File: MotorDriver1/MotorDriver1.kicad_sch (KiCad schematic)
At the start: 14 parts, among them J1 REPLACE W STM I/O PIN CONN, J2 REPLACE W STM I/O PIN CONN, Q1 IRLZ44N, Q2 IRLZ44N

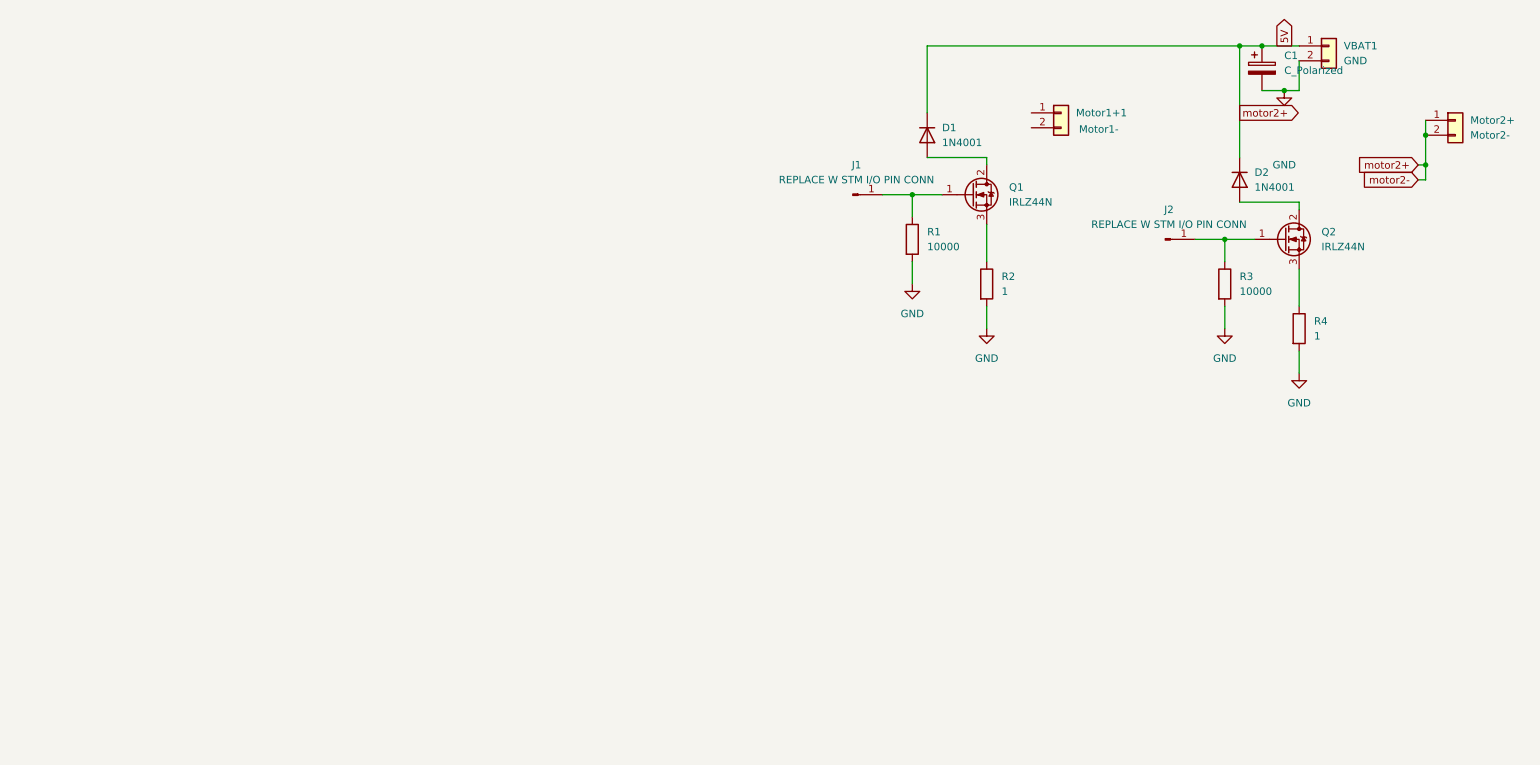
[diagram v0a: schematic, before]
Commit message: Set up KiCad libraries & STM32 page
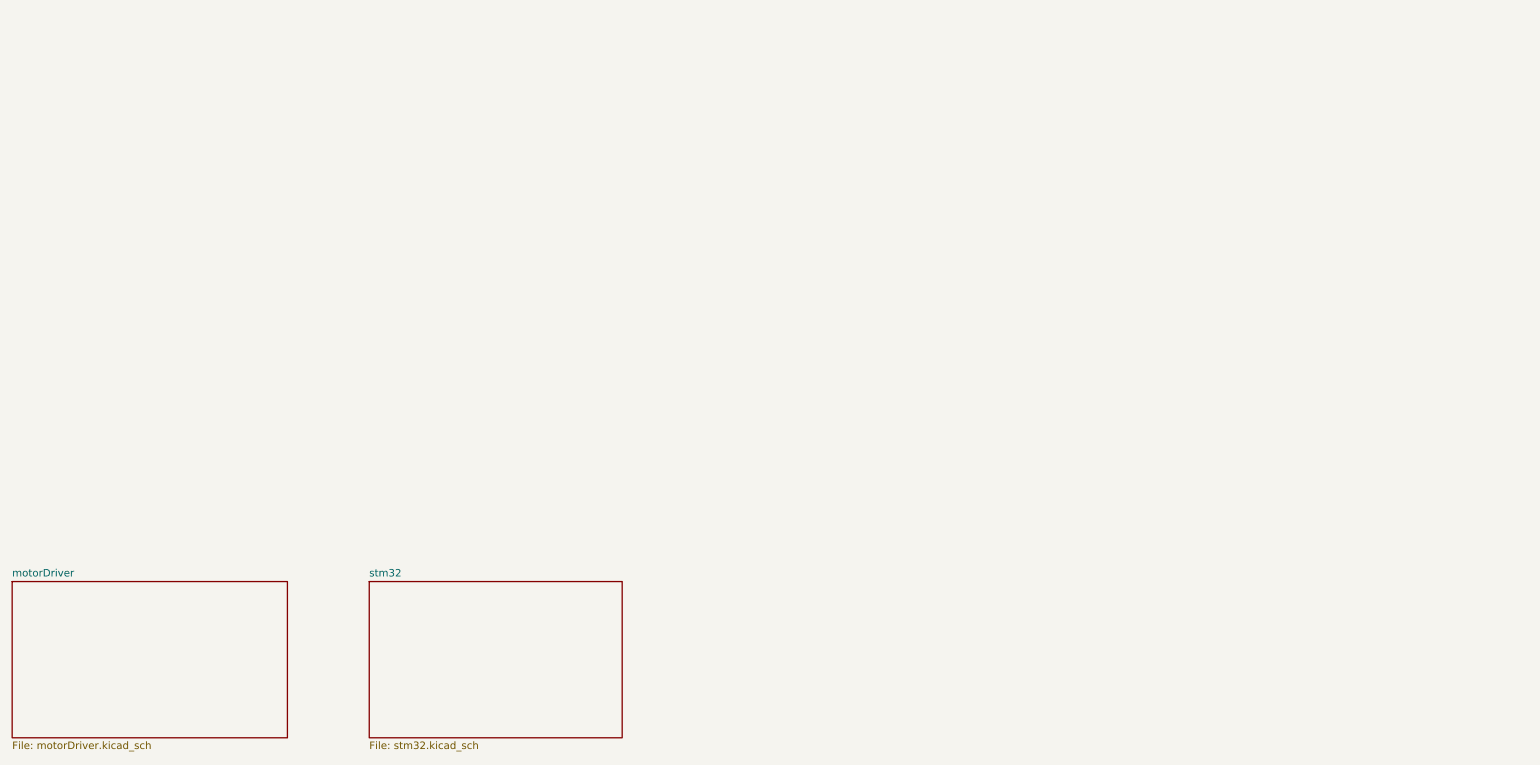
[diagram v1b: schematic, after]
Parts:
- removed C1: C_Polarized, symbol Device:C_Polarized
- removed D1, D2: 1N4001, Diode_THT:D_DO-41_SOD81_P10.16mm_Horizontal, symbol Diode:1N4001
- removed J1, J2: REPLACE W STM I/O PIN CONN, symbol Connector:Conn_01x01_Pin
- removed Motor1+1: Motor1-, symbol Connector_Generic:Conn_01x02
- removed Motor2+: Motor2-, symbol Connector_Generic:Conn_01x02
- removed Q1, Q2: IRLZ44N, Package_TO_SOT_THT:TO-220-3_Vertical, symbol Transistor_FET:IRLZ44N
- removed R1, R3: 10000, symbol Device:R
- removed R2, R4: 1, symbol Device:R
- removed VBAT1: GND, symbol Connector_Generic:Conn_01x02
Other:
- added sheet motorDriver (motorDriver.kicad_sch)
- added sheet stm32 (stm32.kicad_sch)

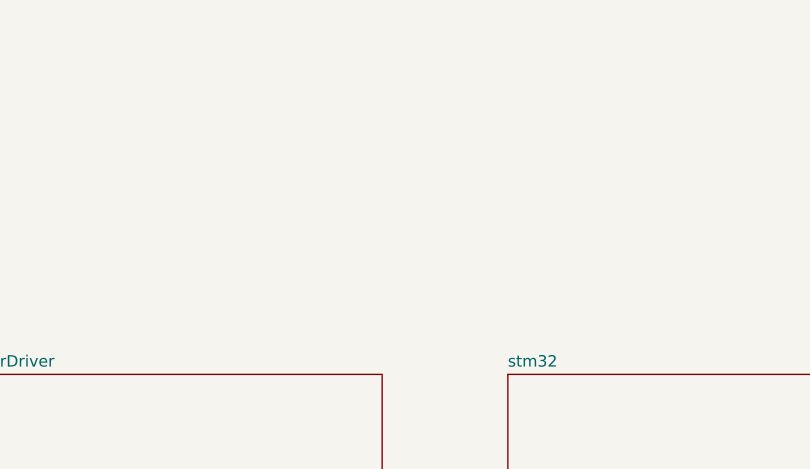
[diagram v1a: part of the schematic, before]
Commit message: added pressure sensor and flags to STM need op amp rails
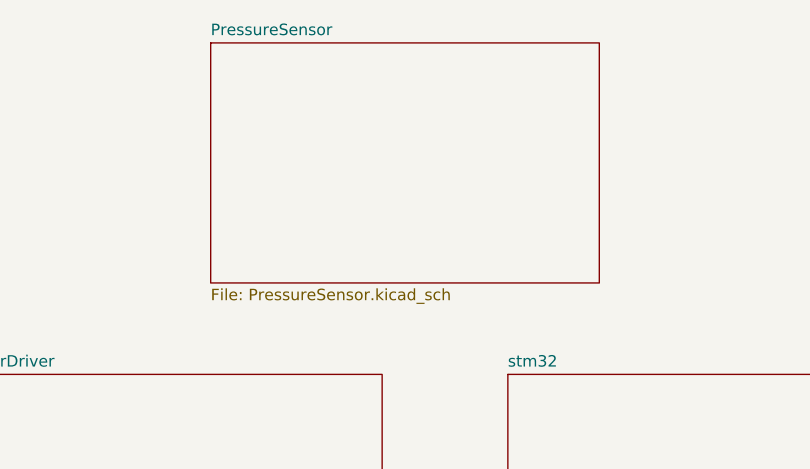
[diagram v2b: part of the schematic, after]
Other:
- added sheet PressureSensor (PressureSensor.kicad_sch)
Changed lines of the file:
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@@
 	(paper "A4")
+	(sheet
+		(at 52.07 118.11)
+		(size 43.18 26.67)
+		(exclude_from_sim no)
+		(in_bom yes)
+		(on_board yes)
+		(dnp no)
+		(fields_autoplaced yes)
+		(stroke
+			(width 0.1524)
+			(type solid)
+		)
+		(fill
+			(color 0 0 0 0.0000)
+		)
+		(property "Sheetname" "PressureSensor"
+			(at 52.07 117.3984 0)
+			(effects
+				(font
+					(size 1.27 1.27)
+				)
+				(justify left bottom)
+			)
+		)
+		(property "Sheetfile" "PressureSensor.kicad_sch"
+			(at 52.07 145.3646 0)
+			(effects
+				(font
+					(size 1.27 1.27)
+				)
+				(justify left top)
+			)
+		)
+		(instances
+			(project "MotorDriver1"
+				(path "/79cc9cfe-04d6-4d00-aa84-feae66cf8c45"
+					(page "4")
+				)
+			)
+		)
+	)
 	(sheet
 		(at 24.13 154.94)

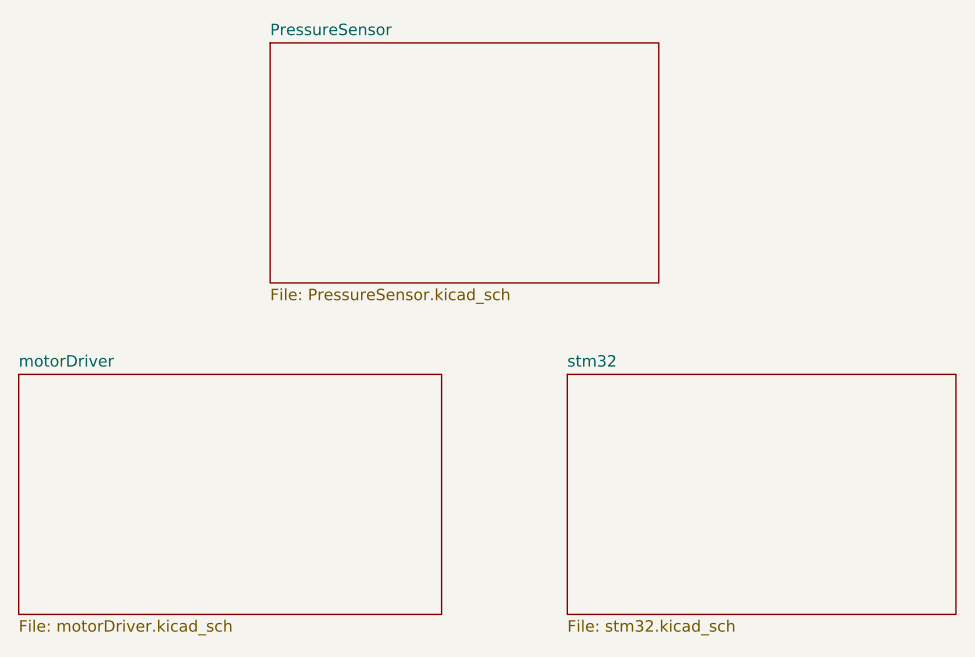
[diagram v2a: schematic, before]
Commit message: missing crystal verification
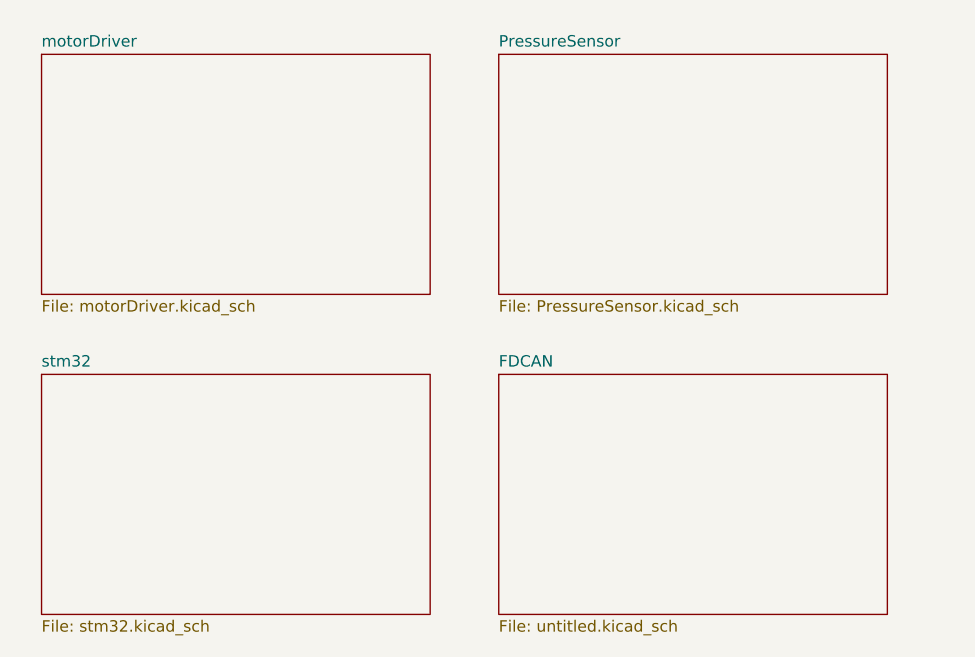
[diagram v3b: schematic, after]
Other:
- added sheet FDCAN (untitled.kicad_sch)
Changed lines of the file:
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@@
 	(paper "A4")
 	(sheet
-		(at 52.07 118.11)
+		(at 77.47 119.38)
 		(size 43.18 26.67)
 		(exclude_from_sim no)
@@
 		)
 		(property "Sheetname" "PressureSensor"
-			(at 52.07 117.3984 0)
+			(at 77.47 118.6684 0)
 			(effects
 				(font
@@
 		)
 		(property "Sheetfile" "PressureSensor.kicad_sch"
-			(at 52.07 145.3646 0)
+			(at 77.47 146.6346 0)
 			(effects
 				(font
@@
 	)
 	(sheet
-		(at 24.13 154.94)
-		(size 46.99 26.67)
+		(at 77.47 154.94)
+		(size 43.18 26.67)
+		(exclude_from_sim no)
+		(in_bom yes)
+		(on_board yes)
+		(dnp no)
+		(fields_autoplaced yes)
+		(stroke
+			(width 0.1524)
+			(type solid)
+		)
+		(fill
+			(color 0 0 0 0.0000)
+		)
+		(property "Sheetname" "FDCAN"
+			(at 77.47 154.2284 0)
+			(effects
+				(font
+					(size 1.27 1.27)
+				)
+				(justify left bottom)
+			)
+		)
+		(property "Sheetfile" "untitled.kicad_sch"
+			(at 77.47 182.1946 0)
+			(effects
+				(font
+					(size 1.27 1.27)
+				)
+				(justify left top)
+			)
+		)
+		(instances
+			(project "MotorDriver1"
+				(path "/79cc9cfe-04d6-4d00-aa84-feae66cf8c45"
+					(page "5")
+				)
+			)
+		)
+	)
+	(sheet
+		(at 26.67 119.38)
+		(size 43.18 26.67)
 		(exclude_from_sim no)
 		(in_bom yes)
@@
 		)
 		(property "Sheetname" "motorDriver"
-			(at 24.13 154.2284 0)
+			(at 26.67 118.6684 0)
 			(effects
 				(font
@@
 		)
 		(property "Sheetfile" "motorDriver.kicad_sch"
-			(at 24.13 182.1946 0)
+			(at 26.67 146.6346 0)
 			(effects
 				(font
@@
 	)
 	(sheet
-		(at 85.09 154.94)
+		(at 26.67 154.94)
 		(size 43.18 26.67)
 		(exclude_from_sim no)
@@
 		)
 		(property "Sheetname" "stm32"
-			(at 85.09 154.2284 0)
+			(at 26.67 154.2284 0)
 			(effects
 				(font
@@
 		)
 		(property "Sheetfile" "stm32.kicad_sch"
-			(at 85.09 182.1946 0)
+			(at 26.67 182.1946 0)
 			(effects
 				(font

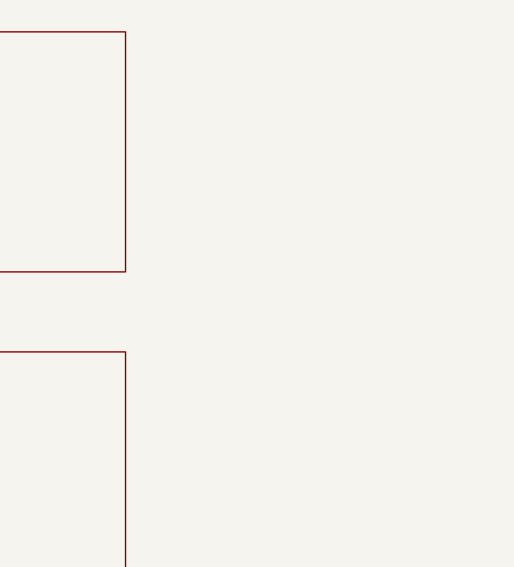
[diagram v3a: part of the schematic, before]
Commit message: Added tooling holes
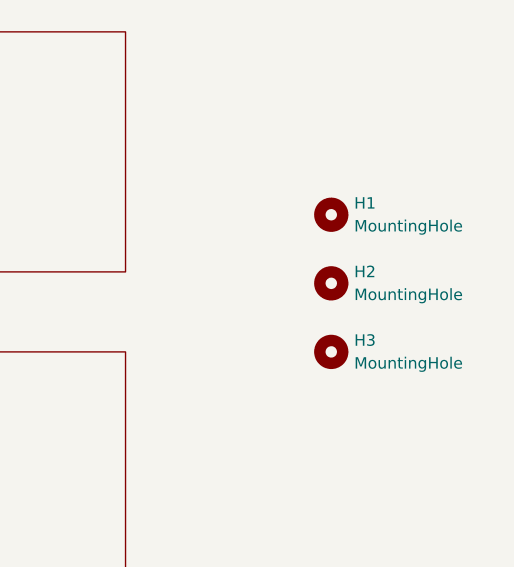
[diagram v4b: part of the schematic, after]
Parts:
- added H1, H2, H3: MountingHole, MountingHole:ToolingHole_1.152mm, symbol Mechanical:MountingHole
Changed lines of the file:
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@@
 	(generator_version "9.0")
 	(paper "A4")
+	(symbol
+		(lib_id "Mechanical:MountingHole")
+		(at 143.51 147.32 0)
+		(unit 1)
+		(exclude_from_sim no)
+		(in_bom no)
+		(on_board yes)
+		(dnp no)
+		(fields_autoplaced yes)
+		(property "Reference" "H2"
+			(at 146.05 146.0499 0)
+			(effects
+				(font
+					(size 1.27 1.27)
+				)
+				(justify left)
+			)
+		)
+		(property "Value" "MountingHole"
+			(at 146.05 148.5899 0)
+			(effects
+				(font
+					(size 1.27 1.27)
+				)
+				(justify left)
+			)
+		)
+		(property "Footprint" "MountingHole:ToolingHole_1.152mm"
+			(at 143.51 147.32 0)
+			(effects
+				(font
+					(size 1.27 1.27)
+				)
+				(hide yes)
+			)
+		)
+		(property "Datasheet" "~"
+			(at 143.51 147.32 0)
+			(effects
+				(font
+					(size 1.27 1.27)
+				)
+				(hide yes)
+			)
+		)
+		(property "Description" "Mounting Hole without connection"
+			(at 143.51 147.32 0)
+			(effects
+				(font
+					(size 1.27 1.27)
+				)
+				(hide yes)
+			)
+		)
+		(instances
+			(project "MotorDriver1"
+				(path "/79cc9cfe-04d6-4d00-aa84-feae66cf8c45"
+					(reference "H2")
+					(unit 1)
+				)
+			)
+		)
+	)
+	(symbol
+		(lib_id "Mechanical:MountingHole")
+		(at 143.51 154.94 0)
+		(unit 1)
+		(exclude_from_sim no)
+		(in_bom no)
+		(on_board yes)
+		(dnp no)
+		(fields_autoplaced yes)
+		(property "Reference" "H3"
+			(at 146.05 153.6699 0)
+			(effects
+				(font
+					(size 1.27 1.27)
+				)
+				(justify left)
+			)
+		)
+		(property "Value" "MountingHole"
+			(at 146.05 156.2099 0)
+			(effects
+				(font
+					(size 1.27 1.27)
+				)
+				(justify left)
+			)
+		)
+		(property "Footprint" "MountingHole:ToolingHole_1.152mm"
+			(at 143.51 154.94 0)
+			(effects
+				(font
+					(size 1.27 1.27)
+				)
+				(hide yes)
+			)
+		)
+		(property "Datasheet" "~"
+			(at 143.51 154.94 0)
+			(effects
+				(font
+					(size 1.27 1.27)
+				)
+				(hide yes)
+			)
+		)
+		(property "Description" "Mounting Hole without connection"
+			(at 143.51 154.94 0)
+			(effects
+				(font
+					(size 1.27 1.27)
+				)
+				(hide yes)
+			)
+		)
+		(instances
+			(project "MotorDriver1"
+				(path "/79cc9cfe-04d6-4d00-aa84-feae66cf8c45"
+					(reference "H3")
+					(unit 1)
+				)
+			)
+		)
+	)
+	(symbol
+		(lib_id "Mechanical:MountingHole")
+		(at 143.51 139.7 0)
+		(unit 1)
+		(exclude_from_sim no)
+		(in_bom no)
+		(on_board yes)
+		(dnp no)
+		(fields_autoplaced yes)
+		(property "Reference" "H1"
+			(at 146.05 138.4299 0)
+			(effects
+				(font
+					(size 1.27 1.27)
+				)
+				(justify left)
+			)
+		)
+		(property "Value" "MountingHole"
+			(at 146.05 140.9699 0)
+			(effects
+				(font
+					(size 1.27 1.27)
+				)
+				(justify left)
+			)
+		)
+		(property "Footprint" "MountingHole:ToolingHole_1.152mm"
+			(at 143.51 139.7 0)
+			(effects
+				(font
+					(size 1.27 1.27)
+				)
+				(hide yes)
+			)
+		)
+		(property "Datasheet" "~"
+			(at 143.51 139.7 0)
+			(effects
+				(font
+					(size 1.27 1.27)
+				)
+				(hide yes)
+			)
+		)
+		(property "Description" "Mounting Hole without connection"
+			(at 143.51 139.7 0)
+			(effects
+				(font
+					(size 1.27 1.27)
+				)
+				(hide yes)
+			)
+		)
+		(instances
+			(project ""
+				(path "/79cc9cfe-04d6-4d00-aa84-feae66cf8c45"
+					(reference "H1")
+					(unit 1)
+				)
+			)
+		)
+	)
 	(sheet
 		(at 77.47 119.38)

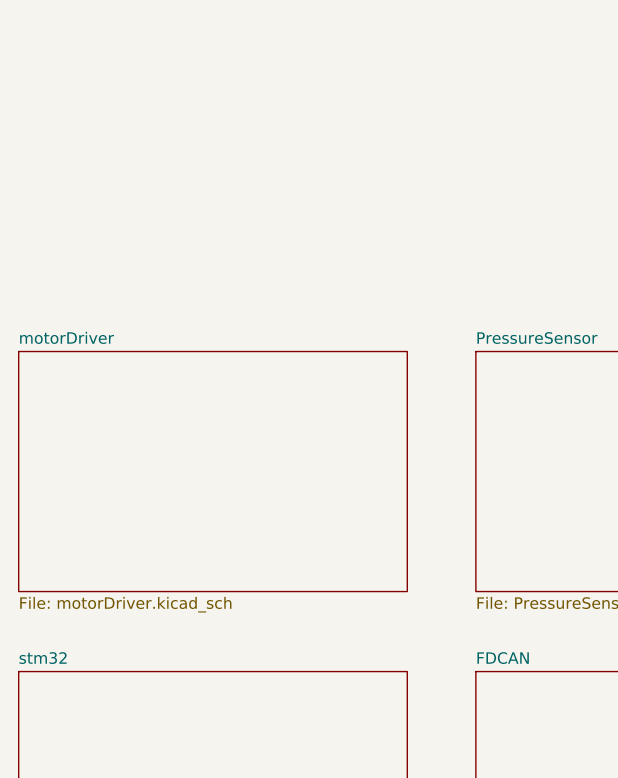
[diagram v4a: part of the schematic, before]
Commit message: added motors and sensors for 4 pad system
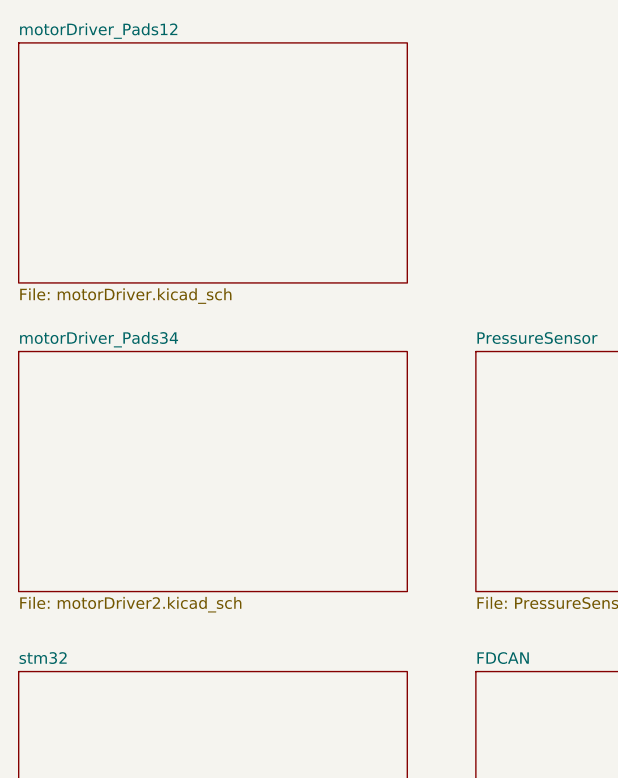
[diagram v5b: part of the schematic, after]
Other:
- sheet motorDriver renamed motorDriver_Pads12
- added sheet motorDriver_Pads34 (motorDriver2.kicad_sch)
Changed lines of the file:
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@@
+	)
+	(sheet
+		(at 26.67 119.38)
+		(size 43.18 26.67)
+		(exclude_from_sim no)
+		(in_bom yes)
+		(on_board yes)
+		(dnp no)
+		(fields_autoplaced yes)
+		(stroke
+			(width 0.1524)
+			(type solid)
+		)
+		(fill
+			(color 0 0 0 0.0000)
+		)
+		(property "Sheetname" "motorDriver_Pads34"
+			(at 26.67 118.6684 0)
+			(effects
+				(font
+					(size 1.27 1.27)
+				)
+				(justify left bottom)
+			)
+		)
+		(property "Sheetfile" "motorDriver2.kicad_sch"
+			(at 26.67 146.6346 0)
+			(effects
+				(font
+					(size 1.27 1.27)
+				)
+				(justify left top)
+			)
+		)
+		(instances
+			(project "MotorDriver1"
+				(path "/79cc9cfe-04d6-4d00-aa84-feae66cf8c45"
+					(page "6")
+				)
+			)
+		)
 	)
 	(sheet
@@
 	)
 	(sheet
-		(at 26.67 119.38)
+		(at 26.67 85.09)
 		(size 43.18 26.67)
 		(exclude_from_sim no)
@@
 		(on_board yes)
 		(dnp no)
-		(fields_autoplaced yes)
 		(stroke
 			(width 0.1524)
@@
 			(color 0 0 0 0.0000)
 		)
-		(property "Sheetname" "motorDriver"
-			(at 26.67 118.6684 0)
+		(property "Sheetname" "motorDriver_Pads12"
+			(at 26.67 84.3784 0)
 			(effects
 				(font
@@
 		)
 		(property "Sheetfile" "motorDriver.kicad_sch"
-			(at 26.67 146.6346 0)
+			(at 26.67 112.3446 0)
 			(effects
 				(font
